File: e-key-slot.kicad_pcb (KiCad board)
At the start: 2 copper layers, 28 x 37.6 mm, 46 parts, among them J1 PJ-018, J2 MDT420E03002, Q1 TSM9409CS, Q2 TSM9409CS, Q3 TSM9409CS, Q4 SSM3J328R_LF, U1 TPS54331DRG4, U2 MCP73831T-5ACI_OT, U4 MT3608

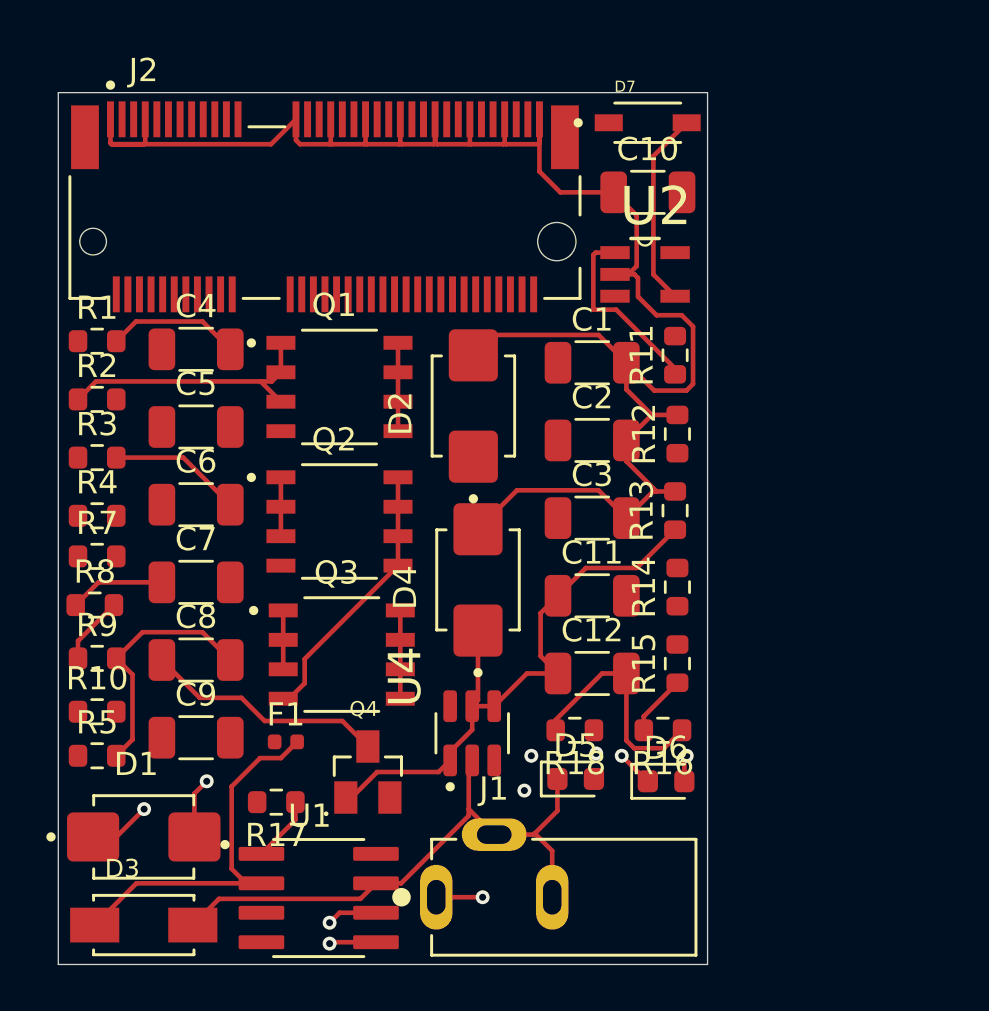
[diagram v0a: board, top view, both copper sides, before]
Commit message: Delete all tracks
Signed-off-by: JeffMboya <jangina.mboya@gmail.com>
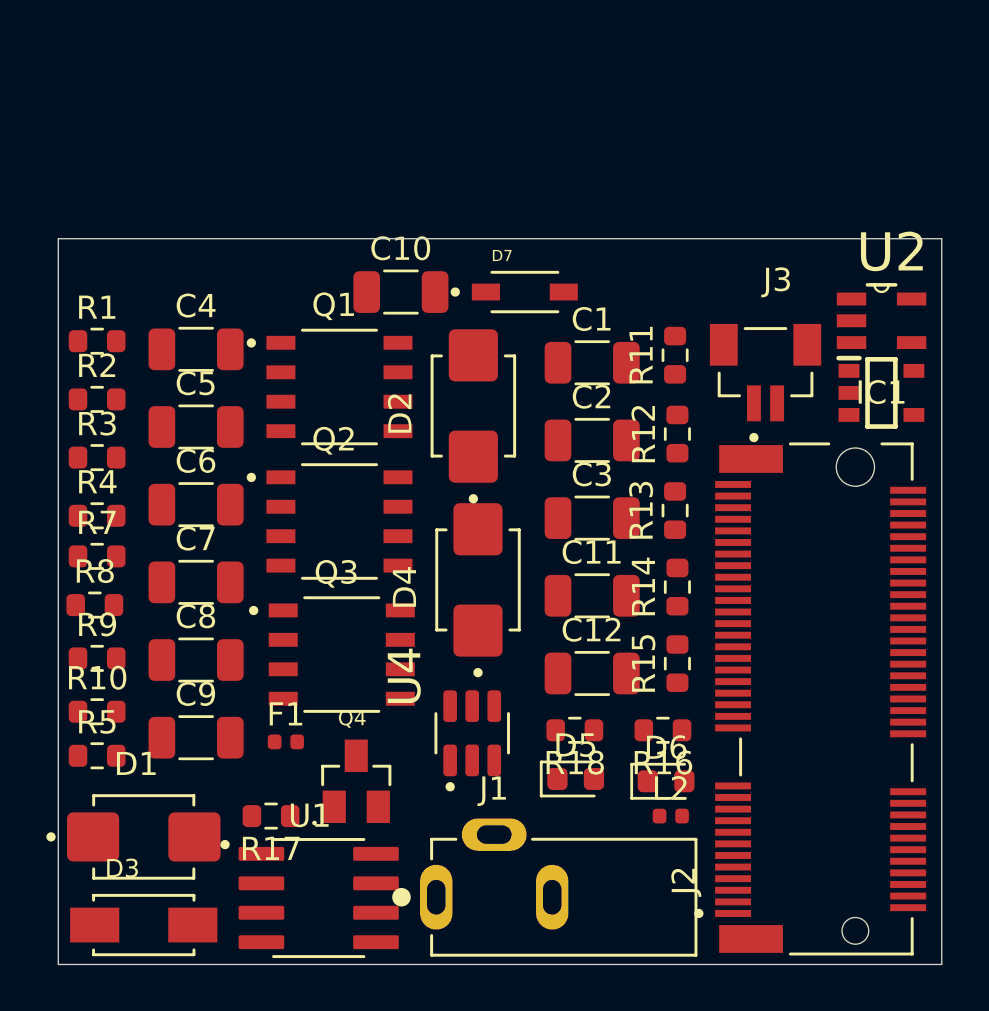
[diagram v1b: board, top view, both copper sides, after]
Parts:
- added IC1: XC6220A331MR-G, XC6220A331MR-G:SOT95P280X120-5N, F.Cu at (114.8, 66.5)
- added J3: BM02B-SRSS-TB_LF__SN_, BM02B-SRSS-TB_LF__SN_:JST_BM02B-SRSS-TB_LF__SN_, F.Cu at (109.8, 64.4)
- added L2: L_Iron, Inductor_SMD:L_0402_1005Metric, F.Cu at (105.7, 84.7)
- moved J2 30.2 mm to (113.7, 79.7), turned to 90 degrees
- moved C10 11.5 mm to (94.1, 62.1)
- moved U2 10.4 mm to (114.8, 63.3)
- moved D7 9.02 mm to (99.4, 62.1)
- moved R17 0.64 mm to (88.5, 84.7)
- moved Q4 0.64 mm to (92.2, 83.2)
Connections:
- C12 pad 1: BOOT -> +5V
- C7 pad 1: BOOT -> +5V
- D6 pad 2: BOOT -> +5V
- D7 pad A: BOOT -> +5V
- Q4 pad 1: BOOT -> +5V
- R13 pad 1: BOOT -> +5V
- R17 pad 1: BOOT -> +5V
- U2 pad 4: BOOT -> +5V
- U4 pad 1: BOOT -> +5V
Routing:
- net VSS: track 136.6 -> 0.00 mm
- net BOOT: track 42.3 -> 0.00 mm, vias 1 -> 0
- net Net-(D1-PadC): track 19.5 -> 0.00 mm, vias 1 -> 0
- net Vin: track 16.7 -> 0.00 mm
- net Net-(Q2-Pad5): track 11.7 -> 0.00 mm
- net +BATT: track 10.4 -> 0.00 mm
- net Net-(U2-STAT): track 8.16 -> 0.00 mm
- net Net-(J1-Pad1): track 5.81 -> 0.00 mm, vias 1 -> 0
- net VSENCE: track 4.97 -> 0.00 mm, vias 1 -> 0
- net Net-(F1-Pad1): track 3.81 -> 0.00 mm
- net BATT_MON: track 2.65 -> 0.00 mm
- net Net-(D1-PadA): track 2.62 -> 0.00 mm, vias 1 -> 0
- net COMP: track 2.36 -> 0.00 mm, vias 1 -> 0
- net Net-(D6-K): track 1.58 -> 0.00 mm, vias 1 -> 0
- net (no net): vias 3 -> 0
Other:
- board size 28 x 37.6 mm -> 38.1 x 31.3 mm

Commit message: Update component placement
Signed-off-by: JeffMboya <jangina.mboya@gmail.com>
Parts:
- moved U2 28.7 mm to (86.2, 65.7), turned to 90 degrees
- moved D7 19.2 mm to (80.6, 66.0), turned to 90 degrees
- moved C10 11.5 mm to (83.2, 65.8), turned to 90 degrees
- moved R1 5.38 mm to (80.9, 69.6)
- moved C4 5.05 mm to (84.8, 69.6)
- moved D6 4.70 mm to (100.8, 83.2)
- moved R2 4.47 mm to (80.9, 71.2)
- moved C5 4.30 mm to (84.8, 72.2)
- moved L2 3.91 mm to (106.0, 80.8)
- moved R3 3.56 mm to (80.9, 72.8)
- moved C6 3.45 mm to (84.9, 74.7)
- moved C7 2.71 mm to (84.8, 77.3)
- moved R4 2.65 mm to (80.9, 74.4)
- moved R7 2.50 mm to (80.9, 76.0)
- moved C12 2.05 mm to (102.4, 76.5)
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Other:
- board size 38.1 x 31.3 mm -> 37.8 x 27.8 mm

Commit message: Convert from 2 to 4 layers
Signed-off-by: JeffMboya <jangina.mboya@gmail.com>
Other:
- copper layers 2 -> 4
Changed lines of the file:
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@@
 	(layers
 		(0 "F.Cu" signal)
+		(1 "In1.Cu" signal)
+		(2 "In2.Cu" signal)
 		(31 "B.Cu" signal)
 		(32 "B.Adhes" user "B.Adhesive")
@@
 	)
 	(setup
+		(stackup
+			(layer "F.SilkS"
+				(type "Top Silk Screen")
+			)
+			(layer "F.Paste"
+				(type "Top Solder Paste")
+			)
+			(layer "F.Mask"
+				(type "Top Solder Mask")
+				(thickness 0.01)
+			)
+			(layer "F.Cu"
+				(type "copper")
+				(thickness 0.035)
+			)
+			(layer "dielectric 1"
+				(type "prepreg")
+				(thickness 0.1)
+				(material "FR4")
+				(epsilon_r 4.5)
+				(loss_tangent 0.02)
+			)
+			(layer "In1.Cu"
+				(type "copper")
+				(thickness 0.035)
+			)
+			(layer "dielectric 2"
+				(type "core")
+				(thickness 1.24)
+				(material "FR4")
+				(epsilon_r 4.5)
+				(loss_tangent 0.02)
+			)
+			(layer "In2.Cu"
+				(type "copper")
+				(thickness 0.035)
+			)
+			(layer "dielectric 3"
+				(type "prepreg")
+				(thickness 0.1)
+				(material "FR4")
+				(epsilon_r 4.5)
+				(loss_tangent 0.02)
+			)
+			(layer "B.Cu"
+				(type "copper")
+				(thickness 0.035)
+			)
+			(layer "B.Mask"
+				(type "Bottom Solder Mask")
+				(thickness 0.01)
+			)
+			(layer "B.Paste"
+				(type "Bottom Solder Paste")
+			)
+			(layer "B.SilkS"
+				(type "Bottom Silk Screen")
+			)
+			(copper_finish "None")
+			(dielectric_constraints no)
+		)
 		(pad_to_mask_clearance 0)
 		(allow_soldermask_bridges_in_footprints no)

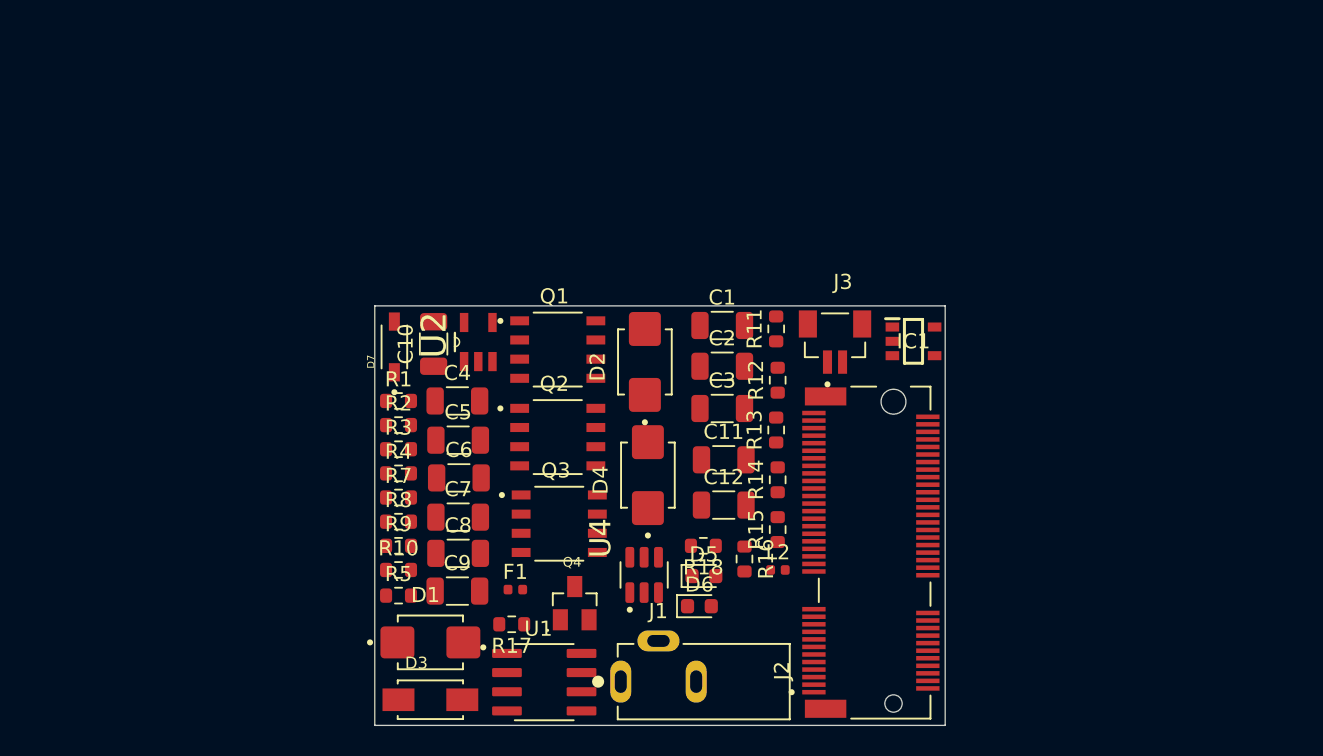
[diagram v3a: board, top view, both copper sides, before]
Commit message: Replace dual holder with single holder
Signed-off-by: JeffMboya <jangina.mboya@gmail.com>
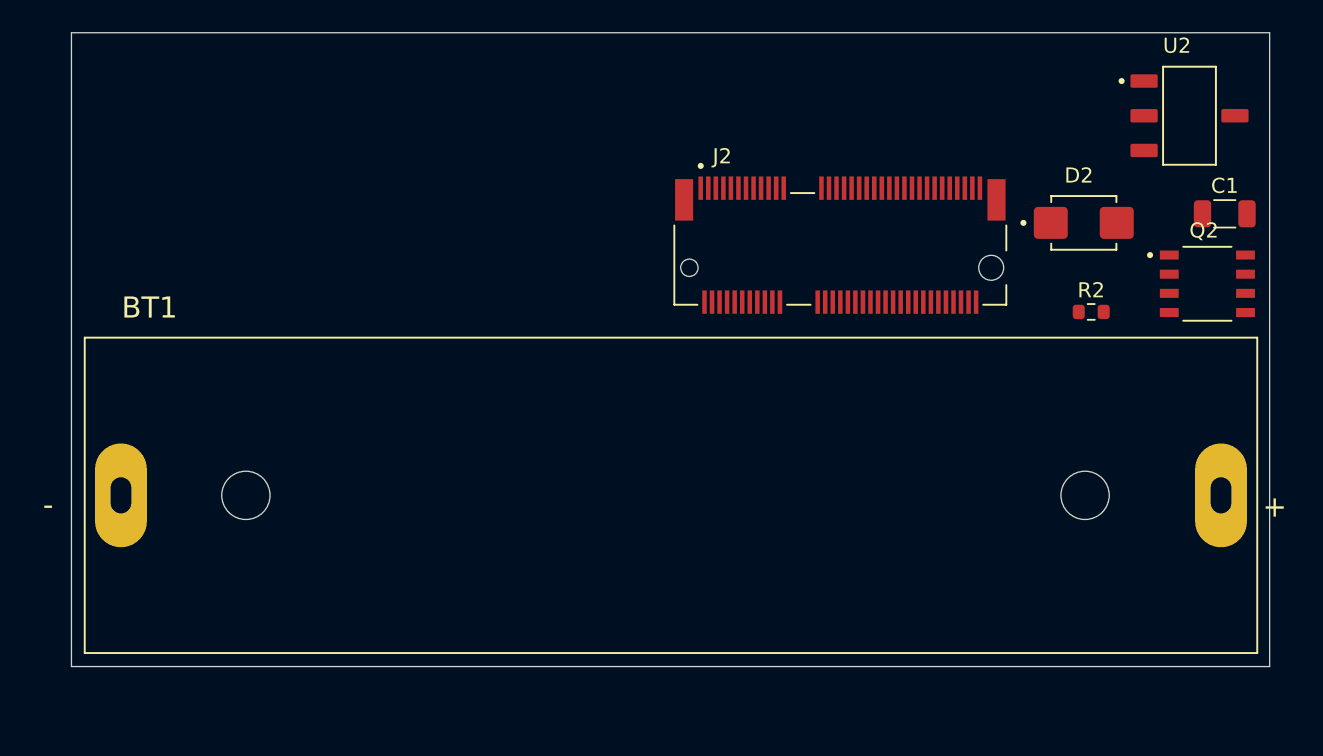
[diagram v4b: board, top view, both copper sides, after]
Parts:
- removed C10, C8, C9: 10uF, Capacitor_SMD:C_1206_3216Metric
- removed C11, C12: 22uF, Capacitor_SMD:C_1206_3216Metric
- removed C2: 10pF, Capacitor_SMD:C_1206_3216Metric
- removed C3: 1.5nF, Capacitor_SMD:C_1206_3216Metric
- removed C4: 8.2nF, Capacitor_SMD:C_1206_3216Metric
- removed C5, C6: 100nF, Capacitor_SMD:C_1206_3216Metric
- removed C7: 4.7uF, Capacitor_SMD:C_1206_3216Metric
- removed D1, D4: 1SMB5931BT3G, 1SMB5931BT3G:DIOM5436X247N
- removed D3: SMAJ10CA, SMAJ10CA:DIOM4325X250N
- removed D5, D6: LED, LED_SMD:LED_0603_1608Metric
- removed D7: 1N5819HW-7-F, 1N5819HW-7-F:SOD3715X145N
- removed F1: Fuse, Fuse:Fuse_0402_1005Metric
- removed IC1: XC6220A331MR-G, XC6220A331MR-G:SOT95P280X120-5N
- removed J1: PJ-018, PJ-018:CUI_PJ-018
- removed J3: BM02B-SRSS-TB_LF__SN_, BM02B-SRSS-TB_LF__SN_:JST_BM02B-SRSS-TB_LF__SN_
- removed L2: L_Iron, Inductor_SMD:L_0402_1005Metric
- removed Q1, Q3: TSM9409CS, TSM9409CS:TRANS_TSM9409CS
- removed Q4: SSM3J328R_LF, SSM3J328R_LF:SOT95P240X88-3N
- removed R1, R10, R3: 100, Resistor_SMD:R_0603_1608Metric
- removed R11, R12, R13, R14: 10k, Resistor_SMD:R_0603_1608Metric
- removed R15, R16: 100k, Resistor_SMD:R_0603_1608Metric
- removed R17: 22k, Resistor_SMD:R_0603_1608Metric
- removed R18: 2.2k, Resistor_SMD:R_0603_1608Metric
- removed R4: 169k, Resistor_SMD:R_0603_1608Metric
- removed R5: 31.6k, Resistor_SMD:R_0603_1608Metric
- removed R7: 18.7k, Resistor_SMD:R_0603_1608Metric
- removed R8: 10.2K, Resistor_SMD:R_0603_1608Metric
- removed R9: 3.24K, Resistor_SMD:R_0603_1608Metric
- removed U1: TPS54331DRG4, TPS54331DRG4:SOIC127P599X175-8N
- removed U4: MT3608, MT3608:SOT95P280X145-6N
- added BT1: BH-18650-PC, BH-18650-PC:BAT_BH-18650-PC, F.Cu at (98.9, 75.9)
- U2: value MCP73831T-5ACI_OT -> ZLDO1117G33TA; footprint MCP73831T-5ACI_OT:SOT95P280X145-5N -> ZLDO1117G33TA:SOT230P700X180-4N
- moved U2 49.5 mm to (133.3, 50.7), turned to 0 degrees
- moved R2 46.5 mm to (126.8, 63.7)
- moved Q2 44.2 mm to (134.5, 61.8)
- moved C1 34.1 mm to (135.6, 57.2)
- moved D2 30.5 mm to (126.3, 57.8), turned to 0 degrees
- moved J2 19.2 mm to (110.2, 60.8), turned to 0 degrees
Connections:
- C1 pad 1: Vin -> Net-(BT1-PadP)
- C1 pad 2: VSS -> GND
- D2 pad A: VSS -> Net-(D2-PadA)
- D2 pad C: Net-(D2-PadC) -> 3.7v
- J2 pad 1: VSS -> GND
- J2 pad 2: BOOT -> +3V3
- J2 pad 33: VSS -> GND
- J2 pad 39: VSS -> GND
- J2 pad 45: VSS -> GND
- J2 pad 51: VSS -> GND
- J2 pad 57: VSS -> GND
- J2 pad 63: VSS -> GND
- J2 pad 69: VSS -> GND
- J2 pad 7: VSS -> GND
- J2 pad 75: VSS -> GND
- Q2 pad 1: Net-(D1-PadC) -> 3.7v
- Q2 pad 2: Net-(D1-PadC) -> 3.7v
- Q2 pad 3: Net-(D1-PadC) -> 3.7v
- Q2 pad 4: Net-(D2-PadC) -> Net-(D2-PadA)
- Q2 pad 5: Net-(Q2-Pad5) -> Net-(BT1-PadP)
- Q2 pad 6: Net-(Q2-Pad5) -> Net-(BT1-PadP)
- Q2 pad 7: Net-(Q2-Pad5) -> Net-(BT1-PadP)
- Q2 pad 8: Net-(Q2-Pad5) -> Net-(BT1-PadP)
- R2 pad 1: Net-(D1-PadC) -> Net-(D2-PadA)
- R2 pad 2: Net-(D2-PadC) -> GND
- U2 pad 1: Net-(U2-STAT) -> GND
- U2 pad 2: VSS -> 3.3v
- U2 pad 3: +BATT -> 3.7v
- U2 pad 4: +5V -> 3.3v
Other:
- board size 37.8 x 27.8 mm -> 79.4 x 42 mm

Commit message: Use JST
Signed-off-by: JeffMboya <jangina.mboya@gmail.com>
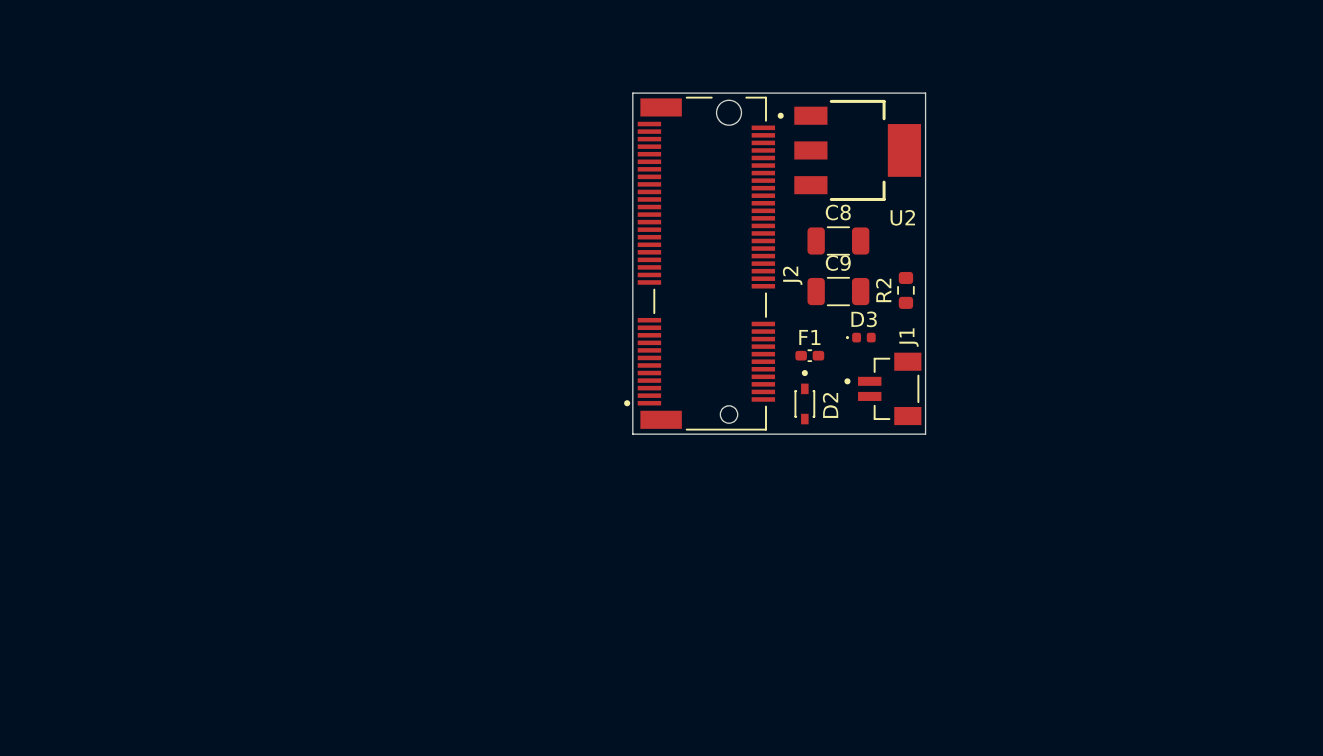
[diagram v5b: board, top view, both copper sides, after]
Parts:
- removed BT1: BH-18650-PC, BH-18650-PC:BAT_BH-18650-PC
- removed C1: 22uF, Capacitor_SMD:C_1206_3216Metric
- removed Q2: TSM9409CS, TSM9409CS:TRANS_TSM9409CS
- added C8: 10uF, Capacitor_SMD:C_1206_3216Metric, F.Cu at (110.0, 59.0)
- added C9: 10uF, Capacitor_SMD:C_1206_3216Metric, F.Cu at (110.0, 62.4)
- added D3: LED, LED_SMD:LED_0402_1005Metric, F.Cu at (111.7, 65.4)
- added F1: Fuse, Fuse:Fuse_0402_1005Metric_Pad0.77x0.64mm_HandSolder, F.Cu at (108.1, 66.6)
- added J1: BM02B-SRSS-TB_LF__SN_, BM02B-SRSS-TB_LF__SN_:JST_BM02B-SRSS-TB_LF__SN_, F.Cu at (114.6, 68.8)
- D2: value 1SMB5931BT3G -> BZT52C12S; footprint 1SMB5931BT3G:DIOM5436X247N -> BZT52C12S:DIO_BZT52C12S
- U2: value ZLDO1117G33TA -> AZ1117IH-3.3TRG1; footprint ZLDO1117G33TA:SOT230P700X180-4N -> AZ1117IH-3.3TRG1:SOT230P700X185-4N
- moved U2 22.1 mm to (111.3, 53.0)
- moved D2 22.0 mm to (107.8, 69.8), turned to -90 degrees
- moved R2 12.4 mm to (114.5, 62.3), turned to 90 degrees
- moved J2 7.38 mm to (102.8, 60.5), turned to 90 degrees
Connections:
- D2 pad A: Net-(D2-PadA) -> GND
- D2 pad C: 3.7v -> INPUT
- R2 pad 1: Net-(D2-PadA) -> INPUT
- R2 pad 2: GND -> Net-(D3-A)
- U2 pad 2: 3.3v -> +3V3
- U2 pad 3: 3.7v -> INPUT
- U2 pad 4: 3.3v -> unconnected-(U2-VOUT-Pad4)
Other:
- board size 79.4 x 42 mm -> 19.4 x 22.6 mm

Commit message: Complete board routing
Signed-off-by: JeffMboya <jangina.mboya@gmail.com>
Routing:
- net GND: track 0.00 -> 73.1 mm
- net +3V3: track 0.00 -> 21.5 mm, vias 0 -> 1
- net INPUT: track 0.00 -> 20.3 mm
- net VIN: track 0.00 -> 15.3 mm, vias 0 -> 1
- net Net-(D3-A): track 0.00 -> 5.40 mm, vias 0 -> 1
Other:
- copper layers 4 -> 2

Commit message: Add board images
Signed-off-by: JeffMboya <jangina.mboya@gmail.com>
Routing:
- net GND: track 73.1 -> 77.5 mm, vias 0 -> 1
- net VIN: track 15.3 -> 16.0 mm
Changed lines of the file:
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@@
+	)
+	(segment
+		(start 111.5 62.35)
+		(end 111.75 62.35)
+		(width 0.2)
+		(layer "F.Cu")
+		(net 1)
 	)
 	(segment
@@
 	)
 	(segment
+		(start 111.75 62.35)
+		(end 112.9 63.5)
+		(width 0.2)
+		(layer "F.Cu")
+		(net 1)
+	)
+	(segment
 		(start 98.575 52.875)
 		(end 98.45 52.75)
@@
 		(net 1)
 	)
-	(segment
-		(start 107.555 66.345)
-		(end 109.2 64.7)
-		(width 0.2)
-		(layer "F.Cu")
-		(net 58)
-	)
-	(segment
-		(start 107.555 66.6)
-		(end 107.555 66.345)
-		(width 0.2)
-		(layer "F.Cu")
-		(net 58)
-	)
-	(segment
-		(start 107.555 59.995)
-		(end 108.55 59)
-		(width 0.2)
-		(layer "F.Cu")
-		(net 58)
-	)
-	(segment
-		(start 107.555 66.6)
-		(end 107.555 59.995)
-		(width 0.2)
-		(layer "F.Cu")
-		(net 58)
-	)
 	(via
-		(at 109.2 64.7)
+		(at 112.9 63.5)
 		(size 0.6)
 		(drill 0.3)
 		(layers "F.Cu" "B.Cu")
-		(net 58)
-	)
-	(segment
-		(start 109.2 64.7)
+		(net 1)
+	)
+	(segment
+		(start 111.3 65.1)
+		(end 111.3 65.4)
+		(width 0.2)
+		(layer "B.Cu")
+		(net 1)
+	)
+	(segment
+		(start 112.9 63.5)
+		(end 111.3 65.1)
+		(width 0.2)
+		(layer "B.Cu")
+		(net 1)
+	)
+	(segment
+		(start 109 64.5)
+		(end 108.8 64.5)
+		(width 0.2)
+		(layer "F.Cu")
+		(net 58)
+	)
+	(segment
+		(start 108.8 64.5)
+		(end 107.555 65.745)
+		(width 0.2)
+		(layer "F.Cu")
+		(net 58)
+	)
+	(segment
+		(start 107.555 66.6)
+		(end 107.3 66.345)
+		(width 0.2)
+		(layer "F.Cu")
+		(net 58)
+	)
+	(segment
+		(start 107.3 66.345)
+		(end 107.3 60.25)
+		(width 0.2)
+		(layer "F.Cu")
+		(net 58)
+	)
+	(segment
+		(start 107.555 65.745)
+		(end 107.555 66.6)
+		(width 0.2)
+		(layer "F.Cu")
+		(net 58)
+	)
+	(segment
+		(start 107.3 60.25)
+		(end 108.55 59)
+		(width 0.2)
+		(layer "F.Cu")
+		(net 58)
+	)
+	(via
+		(at 109 64.5)
+		(size 0.6)
+		(drill 0.3)
+		(layers "F.Cu" "B.Cu")
+		(net 58)
+	)
+	(segment
+		(start 109 64.5)
 		(end 112.1 67.6)
 		(width 0.2)
@@
 	)
 	(segment
+		(start 113.5 64.1)
+		(end 114.5 63.1)
+		(width 0.2)
+		(layer "F.Cu")
+		(net 59)
+	)
+	(segment
 		(start 110.5 64.8)
-		(end 110.52 64.78)
-		(width 0.2)
-		(layer "F.Cu")
-		(net 59)
-	)
-	(segment
-		(start 112.82 64.78)
-		(end 114.5 63.1)
+		(end 111.2 64.1)
 		(width 0.2)
 		(layer "F.Cu")
@@
 	)
 	(segment
+		(start 111.2 64.1)
+		(end 113.5 64.1)
+		(width 0.2)
+		(layer "F.Cu")
+		(net 59)
+	)
+	(segment
 		(start 110.5 64.8)
 		(end 110.5 57.6)
 		(width 0.2)
 		(layer "F.Cu")
-		(net 59)
-	)
-	(segment
-		(start 110.52 64.78)
-		(end 112.82 64.78)
-		(width 0.2)
-		(layer "F.Cu")

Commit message: Update board routes
Signed-off-by: JeffMboya <jangina.mboya@gmail.com>
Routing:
- net GND: track 77.5 -> 80.1 mm, vias 1 -> 2
